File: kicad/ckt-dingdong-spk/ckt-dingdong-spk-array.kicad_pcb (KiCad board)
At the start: 2 copper layers, 292.1 x 40.6 mm, 162 parts, among them J1 SM04B-SRSS

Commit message: Changed to 5x panel
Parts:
- removed the J1 at (209.0, 40.3)
- removed the J1 at (264.8, 40.3)
- removed the J1 at (236.9, 40.3)
- removed the J1 at (181.0, 40.3)
- removed the J1 at (153.1, 40.3)
- removed the REF** at (10.1, 58.9)
- removed the REF** at (4.99, 27.6)
- removed the REF** at (247.6, 53.0)
- removed the REF** at (273.8, 27.6)
- removed the REF** at (286.9, 24.2)
- removed the REF** at (273.8, 53.0)
- removed the REF** at (6.68, 27.6)
- removed the REF** at (245.9, 53.0)
- removed the REF** at (78.2, 27.6)
- removed the REF** at (286.9, 25.1)
- removed the REF** at (77.4, 53.0)
- removed the REF** at (162.9, 53.0)
- removed the REF** at (10.1, 60.6)
- removed the REF** at (79.1, 27.6)
- removed the REF** at (10.1, 59.8)
- removed the REF** at (286.9, 20.8)
- removed the REF** at (4.99, 50.5) (x2)
- removed the REF** at (190.0, 27.6)
- removed the REF** at (245.9, 27.6)
- removed the REF** at (5.84, 27.6)
- removed the REF** at (218.8, 53.0)
- removed the REF** at (134.1, 27.6)
- removed the REF** at (3.30, 53.0)
- removed the REF** at (134.1, 53.0)
- removed the REF** at (219.6, 27.6)
- removed the REF** at (79.9, 27.6)
- removed the REF** at (135.0, 27.6)
- removed the REF** at (163.7, 27.6)
- removed the REF** at (292.0, 27.6)
- removed the REF** at (161.2, 53.0)
- removed the REF** at (293.7, 53.0)
- removed the REF** at (10.1, 23.4)
- removed the REF** at (10.1, 56.4)
- removed the REF** at (286.9, 21.7)
- removed the REF** at (7.53, 27.6)
- removed the REF** at (294.6, 27.6)
- removed the REF** at (275.5, 53.0)
- removed the REF** at (219.6, 53.0)
- removed the REF** at (162.0, 53.0)
- removed the REF** at (4.99, 30.2) (x2)
- removed the REF** at (286.9, 60.6)
- removed the REF** at (286.9, 56.4)
- removed the REF** at (217.1, 53.0)
- removed the REF** at (24.0, 53.0)
- removed the REF** at (4.14, 53.0)
- removed the REF** at (49.4, 53.0)
- removed the REF** at (292.0, 30.2) (x2)
- removed the REF** at (133.3, 27.6)
- removed the REF** at (289.5, 27.6)
- removed the REF** at (218.8, 27.6)
- removed the REF** at (274.7, 53.0)
- removed the REF** at (105.3, 27.6)
- removed the REF** at (275.5, 27.6)
- removed the REF** at (6.68, 53.0)
- removed the REF** at (273.0, 27.6)
- removed the REF** at (286.9, 22.5)
- removed the REF** at (286.9, 20.0)
- removed the REF** at (286.9, 58.9)
- removed the REF** at (10.1, 20.8)
- removed the REF** at (217.9, 27.6)
- removed the REF** at (291.2, 27.6)
- removed the REF** at (21.5, 27.6)
- removed the REF** at (191.7, 53.0)
- removed the REF** at (10.1, 55.6)
- removed the REF** at (292.9, 53.0)
- removed the REF** at (105.3, 53.0)
- removed the REF** at (51.1, 53.0)
- removed the REF** at (107.9, 27.6)
- removed the REF** at (286.9, 55.6)
- removed the REF** at (107.0, 27.6)
- removed the REF** at (274.7, 27.6)
- removed the REF** at (190.0, 53.0)
- removed the REF** at (189.1, 53.0)
- removed the REF** at (10.1, 24.2)
- removed the REF** at (286.9, 58.1)
- removed the REF** at (10.1, 20.0)
- removed the REF** at (273.0, 53.0)
- removed the REF** at (293.7, 27.6)
- removed the REF** at (78.2, 53.0)
- removed the REF** at (107.0, 53.0)
- removed the REF** at (2.45, 27.6)
- removed the REF** at (4.14, 27.6)
- removed the REF** at (190.8, 53.0)
- removed the REF** at (49.4, 27.6)
- removed the REF** at (106.2, 27.6)
- removed the REF** at (23.2, 53.0)
- removed the REF** at (246.7, 27.6)
- removed the REF** at (161.2, 27.6)
- removed the REF** at (162.0, 27.6)
- removed the REF** at (50.3, 27.6)
- removed the REF** at (294.6, 53.0)
- removed the REF** at (10.1, 21.7)
- removed the REF** at (24.0, 27.6)
- removed the REF** at (246.7, 53.0)
- removed the REF** at (286.9, 23.4)
- removed the REF** at (135.8, 27.6)
- removed the REF** at (190.8, 27.6)
- removed the REF** at (191.7, 27.6)
- removed the REF** at (107.9, 53.0)
- removed the REF** at (22.3, 53.0)
- removed the REF** at (52.0, 53.0)
- removed the REF** at (290.3, 53.0)
- removed the REF** at (52.0, 27.6)
- removed the REF** at (290.3, 27.6)
- removed the REF** at (10.1, 57.3)
- removed the REF** at (292.0, 53.0)
- removed the REF** at (289.5, 53.0)
- removed the REF** at (10.1, 22.5)
- removed the REF** at (7.53, 53.0)
- removed the REF** at (21.5, 53.0)
- removed the REF** at (291.2, 53.0)
- removed the REF** at (135.8, 53.0)
- removed the REF** at (2.45, 53.0)
- removed the REF** at (133.3, 53.0)
- removed the REF** at (106.2, 53.0)
- removed the REF** at (135.0, 53.0)
- removed the REF** at (5.84, 53.0)
- removed the REF** at (245.0, 53.0)
- removed the REF** at (247.6, 27.6)
- removed the REF** at (162.9, 27.6)
- removed the REF** at (51.1, 27.6)
- removed the REF** at (10.1, 25.1)
- removed the REF** at (189.1, 27.6)
- removed the REF** at (22.3, 27.6)
- removed the REF** at (79.1, 53.0)
- removed the REF** at (10.1, 58.1)
- removed the REF** at (79.9, 53.0)
- removed the REF** at (50.3, 53.0)
- removed the REF** at (217.9, 53.0)
- removed the REF** at (4.99, 53.0)
- removed the REF** at (23.2, 27.6)
- removed the REF** at (286.9, 57.3)
- removed the REF** at (163.7, 53.0)
- removed the REF** at (245.0, 27.6)
- removed the REF** at (3.30, 27.6)
- removed the REF** at (286.9, 59.8)
- removed the REF** at (292.9, 27.6)
- removed the REF** at (77.4, 27.6)
- removed the REF** at (217.1, 27.6)
- removed the SPK1 at (190.4, 37.8)
- removed the SPK1 at (246.3, 37.8)
- removed the SPK1 at (274.2, 37.8)
- removed the SPK1 at (218.3, 37.8)
- added REF**: NPTH, NPTH, F.Cu at (164.0, 22.6)
- added REF**: NPTH, NPTH, F.Cu at (159.8, 15.8)
- added REF**: Fiducial, Fiducial, B.Cu at (17.5, 45.5)
- added REF**: Fiducial, Fiducial, B.Cu at (17.5, 25.2)
- added REF**: Fiducial, Fiducial, B.Cu at (164.9, 25.2)
- added REF**: NPTH, NPTH, F.Cu at (34.0, 22.6)
- added REF**: NPTH, NPTH, F.Cu at (166.6, 48.0)
- added REF**: NPTH, NPTH, F.Cu at (22.6, 55.6)
- added REF**: NPTH, NPTH, F.Cu at (64.5, 48.0)
- added REF**: NPTH, NPTH, F.Cu at (22.6, 15.8)
- added REF**: NPTH, NPTH, F.Cu at (34.9, 48.0)
- added REF**: NPTH, NPTH, F.Cu at (166.6, 22.6)
- added REF**: NPTH, NPTH, F.Cu at (159.8, 55.6)
- added REF**: NPTH, NPTH, F.Cu at (162.3, 22.6)
- added REF**: NPTH, NPTH, F.Cu at (22.6, 54.8)
- added REF**: NPTH, NPTH, F.Cu at (162.3, 48.0)
- added REF**: NPTH, NPTH, F.Cu at (119.6, 48.0)
- added REF**: NPTH, NPTH, F.Cu at (159.8, 54.8)
- added REF**: NPTH, NPTH, F.Cu at (145.8, 48.0)
- added REF**: NPTH, NPTH, F.Cu at (15.8, 22.6)
- added REF**: NPTH, NPTH, F.Cu at (119.6, 22.6)
- added REF**: NPTH, NPTH, F.Cu at (16.7, 48.0)
- added REF**: NPTH, NPTH, F.Cu at (35.7, 48.0)
- added REF**: NPTH, NPTH, F.Cu at (20.1, 22.6)
- added REF**: NPTH, NPTH, F.Cu at (92.5, 22.6)
- added REF**: NPTH, NPTH, F.Cu at (22.6, 17.5)
- added REF**: NPTH, NPTH, F.Cu at (22.6, 18.4)
- added REF**: NPTH, NPTH, F.Cu at (159.8, 50.6)
- added REF**: NPTH, NPTH, F.Cu at (118.7, 22.6)
- added REF**: NPTH, NPTH, F.Cu at (62.0, 48.0)
- added REF**: NPTH, NPTH, F.Cu at (159.8, 53.1)
- added REF**: NPTH, NPTH, F.Cu at (159.8, 53.9)
- added REF**: NPTH, NPTH, F.Cu at (165.7, 22.6)
- added REF**: NPTH, NPTH, F.Cu at (64.5, 22.6)
- added REF**: NPTH, NPTH, F.Cu at (165.7, 48.0)
- added REF**: NPTH, NPTH, F.Cu at (15.0, 22.6)
- added REF**: NPTH, NPTH, F.Cu at (148.3, 22.6)
- added REF**: NPTH, NPTH, F.Cu at (16.7, 22.6)
- added REF**: NPTH, NPTH, F.Cu at (147.5, 22.6)
- added REF**: NPTH, NPTH, F.Cu at (163.2, 22.6)
- added REF**: NPTH, NPTH, F.Cu at (145.8, 22.6)
- added REF**: NPTH, NPTH, F.Cu at (146.7, 48.0)
- added REF**: NPTH, NPTH, F.Cu at (63.7, 48.0)
- added REF**: NPTH, NPTH, F.Cu at (22.6, 19.2)
- added REF**: NPTH, NPTH, F.Cu at (62.0, 22.6)
- added REF**: NPTH, NPTH, F.Cu at (164.0, 48.0)
- added REF**: NPTH, NPTH, F.Cu at (117.9, 48.0)
- added REF**: NPTH, NPTH, F.Cu at (90.8, 22.6)
- added REF**: NPTH, NPTH, F.Cu at (62.8, 48.0)
- added REF**: NPTH, NPTH, F.Cu at (120.4, 22.6)
- added REF**: NPTH, NPTH, F.Cu at (90.8, 48.0)
- added REF**: NPTH, NPTH, F.Cu at (159.8, 18.4)
- added REF**: NPTH, NPTH, F.Cu at (18.4, 48.0)
- added REF**: NPTH, NPTH, F.Cu at (22.6, 16.7)
- added REF**: Fiducial, Fiducial, F.Cu at (164.9, 25.2)
- added REF**: NPTH, NPTH, F.Cu at (159.8, 52.3)
- added REF**: NPTH, NPTH, F.Cu at (22.6, 15.0)
- added REF**: NPTH, NPTH, F.Cu at (15.8, 48.0)
- added REF**: NPTH, NPTH, F.Cu at (117.9, 22.6)
- added REF**: NPTH, NPTH, F.Cu at (20.1, 48.0)
- added REF**: NPTH, NPTH, F.Cu at (159.8, 16.7)
- added REF**: NPTH, NPTH, F.Cu at (164.9, 22.6)
- added REF**: NPTH, NPTH, F.Cu at (22.6, 51.4)
- added REF**: NPTH, NPTH, F.Cu at (22.6, 53.9)
- added REF**: NPTH, NPTH, F.Cu at (63.7, 22.6)
- added REF**: NPTH, NPTH, F.Cu at (17.5, 22.6)
- added REF**: NPTH, NPTH, F.Cu at (159.8, 19.2)
- added REF**: NPTH, NPTH, F.Cu at (19.2, 48.0)
- added REF**: Fiducial, Fiducial, F.Cu at (17.5, 25.2)
- added REF**: NPTH, NPTH, F.Cu at (147.5, 48.0)
- added REF**: NPTH, NPTH, F.Cu at (89.9, 22.6)
- added REF**: NPTH, NPTH, F.Cu at (15.0, 48.0)
- added REF**: NPTH, NPTH, F.Cu at (62.8, 22.6)
- added REF**: NPTH, NPTH, F.Cu at (36.6, 22.6)
- added REF**: NPTH, NPTH, F.Cu at (159.8, 20.1)
- added REF**: NPTH, NPTH, F.Cu at (148.3, 48.0)
- added REF**: NPTH, NPTH, F.Cu at (17.5, 48.0)
- added REF**: NPTH, NPTH, F.Cu at (22.6, 52.3)
- added REF**: NPTH, NPTH, F.Cu at (34.9, 22.6)
- added REF**: NPTH, NPTH, F.Cu at (19.2, 22.6)
- added REF**: NPTH, NPTH, F.Cu at (159.8, 51.4)
- added REF**: NPTH, NPTH, F.Cu at (164.9, 48.0)
- added REF**: NPTH, NPTH, F.Cu at (159.8, 15.0)
- added REF**: NPTH, NPTH, F.Cu at (22.6, 50.6)
- added REF**: NPTH, NPTH, F.Cu at (146.7, 22.6)
- added REF**: NPTH, NPTH, F.Cu at (92.5, 48.0)
- added REF**: NPTH, NPTH, F.Cu at (22.6, 20.1)
- added REF**: NPTH, NPTH, F.Cu at (118.7, 48.0)
- added REF**: NPTH, NPTH, F.Cu at (18.4, 22.6)
- added REF**: NPTH, NPTH, F.Cu at (89.9, 48.0)
- added REF**: NPTH, NPTH, F.Cu at (163.2, 48.0)
- added REF**: NPTH, NPTH, F.Cu at (36.6, 48.0)
- added REF**: NPTH, NPTH, F.Cu at (34.0, 48.0)
- added REF**: NPTH, NPTH, F.Cu at (91.6, 48.0)
- added REF**: NPTH, NPTH, F.Cu at (22.6, 53.1)
- added REF**: NPTH, NPTH, F.Cu at (91.6, 22.6)
- added REF**: NPTH, NPTH, F.Cu at (167.4, 22.6)
- added REF**: NPTH, NPTH, F.Cu at (120.4, 48.0)
- added REF**: NPTH, NPTH, F.Cu at (35.7, 22.6)
- added REF**: NPTH, NPTH, F.Cu at (167.4, 48.0)
- added REF**: NPTH, NPTH, F.Cu at (159.8, 17.5)
- REF**: renamed from SPK1; value Speaker -> Fiducial; footprint ISE_Generic:Speaker_13x18 -> Fiducial; moved to F.Cu
- moved REF** 145.1 mm to (17.5, 45.5), turned to 0 degrees
- moved J1 13.5 mm to (109.7, 35.3)
- moved J1 13.5 mm to (81.8, 35.3)
- moved SPK1 13.5 mm to (147.1, 32.8)
- moved J1 13.5 mm to (53.9, 35.3)
- moved J1 13.5 mm to (25.9, 35.3)
- moved SPK1 13.5 mm to (35.3, 32.8)
- moved SPK1 13.5 mm to (119.1, 32.8)
- moved SPK1 13.5 mm to (91.2, 32.8)
- moved SPK1 13.5 mm to (63.3, 32.8)
- moved J1 13.5 mm to (137.7, 35.3)
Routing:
- net Board_9-Net-(SPK1-Pad1): track 35.5 -> 0.00 mm, vias 3 -> 0
- net Board_8-Net-(SPK1-Pad1): track 35.5 -> 0.00 mm, vias 3 -> 0
- net Board_7-Net-(SPK1-Pad1): track 35.5 -> 0.00 mm, vias 3 -> 0
- net Board_6-Net-(SPK1-Pad1): track 35.5 -> 0.00 mm, vias 3 -> 0
- net Board_5-Net-(SPK1-Pad1): track 35.5 -> 0.00 mm, vias 3 -> 0
- net Board_9-Net-(SPK1-Pad2): track 21.5 -> 0.00 mm, vias 3 -> 0
- net Board_8-Net-(SPK1-Pad2): track 21.5 -> 0.00 mm, vias 3 -> 0
- net Board_7-Net-(SPK1-Pad2): track 21.5 -> 0.00 mm, vias 3 -> 0
- net Board_6-Net-(SPK1-Pad2): track 21.5 -> 0.00 mm, vias 3 -> 0
- net Board_5-Net-(SPK1-Pad2): track 21.5 -> 0.00 mm, vias 3 -> 0
- removed copper zone on F.Cu, net Board_5-/MP
- removed copper zone on F.Cu, net Board_6-/MP
- removed copper zone on F.Cu, net Board_7-/MP
- removed copper zone on F.Cu, net Board_8-/MP
- removed copper zone on F.Cu, net Board_9-/MP
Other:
- board size 292.1 x 40.6 mm -> 152.4 x 40.6 mm

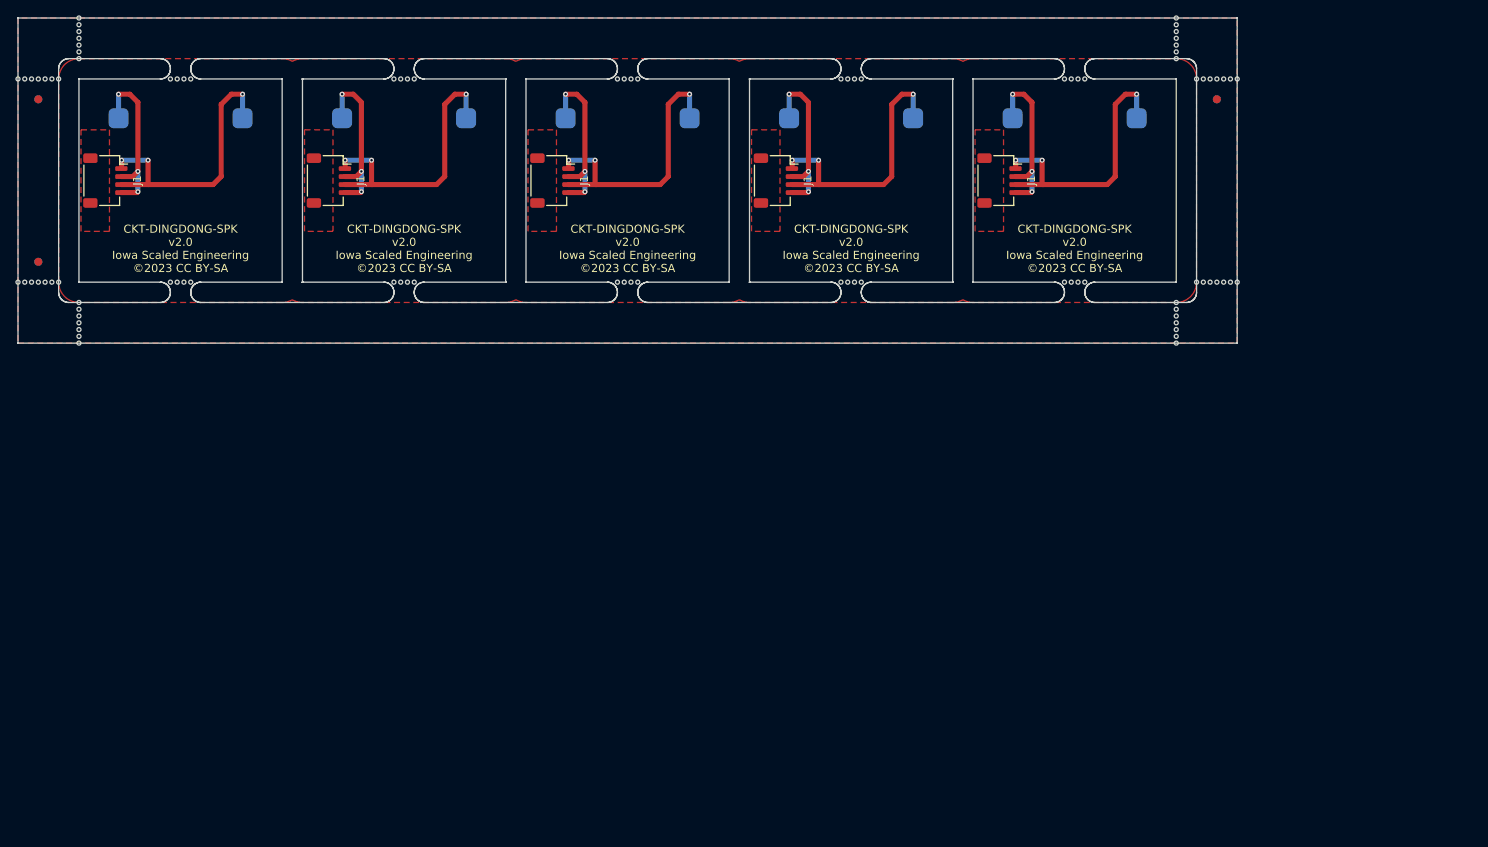
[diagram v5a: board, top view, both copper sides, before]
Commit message: Updated panelization
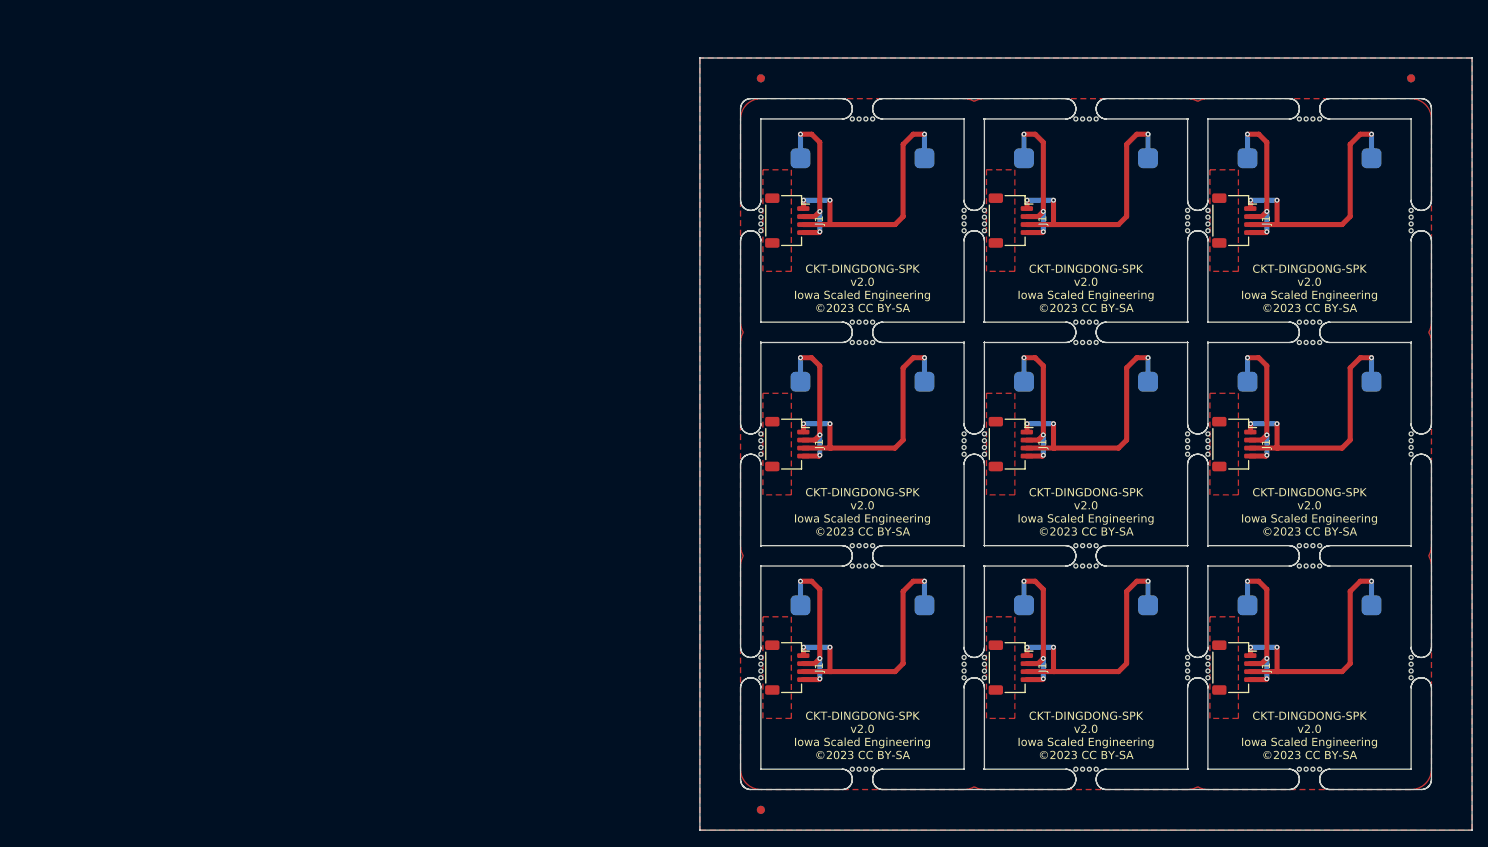
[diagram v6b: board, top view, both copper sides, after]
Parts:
- removed the REF** at (164.0, 22.6)
- removed the REF** at (159.8, 15.8)
- removed the REF** at (17.5, 45.5)
- removed the REF** at (17.5, 25.2) (x2)
- removed the REF** at (164.9, 25.2) (x2)
- removed the REF** at (34.0, 22.6)
- removed the REF** at (166.6, 48.0)
- removed the REF** at (22.6, 55.6)
- removed the REF** at (64.5, 48.0)
- removed the REF** at (22.6, 15.8)
- removed the REF** at (34.9, 48.0)
- removed the REF** at (166.6, 22.6)
- removed the REF** at (159.8, 55.6)
- removed the REF** at (162.3, 22.6)
- removed the REF** at (22.6, 54.8)
- removed the REF** at (162.3, 48.0)
- removed the REF** at (119.6, 48.0)
- removed the REF** at (159.8, 54.8)
- removed the REF** at (145.8, 48.0)
- removed the REF** at (15.8, 22.6)
- removed the REF** at (119.6, 22.6)
- removed the REF** at (16.7, 48.0)
- removed the REF** at (35.7, 48.0)
- removed the REF** at (20.1, 22.6)
- removed the REF** at (92.5, 22.6)
- removed the REF** at (22.6, 17.5)
- removed the REF** at (22.6, 18.4)
- removed the REF** at (159.8, 50.6)
- removed the REF** at (118.7, 22.6)
- removed the REF** at (62.0, 48.0)
- removed the REF** at (159.8, 53.1)
- removed the REF** at (159.8, 53.9)
- removed the REF** at (165.7, 22.6)
- removed the REF** at (64.5, 22.6)
- removed the REF** at (165.7, 48.0)
- removed the REF** at (15.0, 22.6)
- removed the REF** at (148.3, 22.6)
- removed the REF** at (16.7, 22.6)
- removed the REF** at (147.5, 22.6)
- removed the REF** at (163.2, 22.6)
- removed the REF** at (145.8, 22.6)
- removed the REF** at (146.7, 48.0)
- removed the REF** at (63.7, 48.0)
- removed the REF** at (22.6, 19.2)
- removed the REF** at (62.0, 22.6)
- removed the REF** at (164.0, 48.0)
- removed the REF** at (117.9, 48.0)
- removed the REF** at (90.8, 22.6)
- removed the REF** at (62.8, 48.0)
- removed the REF** at (120.4, 22.6)
- removed the REF** at (90.8, 48.0)
- removed the REF** at (159.8, 18.4)
- removed the REF** at (18.4, 48.0)
- removed the REF** at (22.6, 16.7)
- removed the REF** at (159.8, 52.3)
- removed the REF** at (22.6, 15.0)
- removed the REF** at (15.8, 48.0)
- removed the REF** at (117.9, 22.6)
- removed the REF** at (20.1, 48.0)
- removed the REF** at (159.8, 16.7)
- removed the REF** at (164.9, 22.6)
- removed the REF** at (22.6, 51.4)
- removed the REF** at (22.6, 53.9)
- removed the REF** at (63.7, 22.6)
- removed the REF** at (17.5, 22.6)
- removed the REF** at (159.8, 19.2)
- removed the REF** at (19.2, 48.0)
- removed the REF** at (147.5, 48.0)
- removed the REF** at (89.9, 22.6)
- removed the REF** at (15.0, 48.0)
- removed the REF** at (62.8, 22.6)
- removed the REF** at (36.6, 22.6)
- removed the REF** at (159.8, 20.1)
- removed the REF** at (148.3, 48.0)
- removed the REF** at (17.5, 48.0)
- removed the REF** at (22.6, 52.3)
- removed the REF** at (34.9, 22.6)
- removed the REF** at (19.2, 22.6)
- removed the REF** at (159.8, 51.4)
- removed the REF** at (164.9, 48.0)
- removed the REF** at (159.8, 15.0)
- removed the REF** at (22.6, 50.6)
- removed the REF** at (146.7, 22.6)
- removed the REF** at (92.5, 48.0)
- removed the REF** at (22.6, 20.1)
- removed the REF** at (118.7, 48.0)
- removed the REF** at (18.4, 22.6)
- removed the REF** at (89.9, 48.0)
- removed the REF** at (163.2, 48.0)
- removed the REF** at (36.6, 48.0)
- removed the REF** at (34.0, 48.0)
- removed the REF** at (91.6, 48.0)
- removed the REF** at (22.6, 53.1)
- removed the REF** at (91.6, 22.6)
- removed the REF** at (167.4, 22.6)
- removed the REF** at (120.4, 48.0)
- removed the REF** at (35.7, 22.6)
- removed the REF** at (167.4, 48.0)
- removed the REF** at (159.8, 17.5)
- added J1: SM04B-SRSS, Connector_JST:JST_SH_SM04B-SRSS-TB_1x04-1MP_P1.00mm_Horizontal, F.Cu at (139.1, 96.2)
- added J1: SM04B-SRSS, Connector_JST:JST_SH_SM04B-SRSS-TB_1x04-1MP_P1.00mm_Horizontal, F.Cu at (167.0, 96.2)
- added J1: SM04B-SRSS, Connector_JST:JST_SH_SM04B-SRSS-TB_1x04-1MP_P1.00mm_Horizontal, F.Cu at (111.2, 96.2)
- added J1: SM04B-SRSS, Connector_JST:JST_SH_SM04B-SRSS-TB_1x04-1MP_P1.00mm_Horizontal, F.Cu at (167.0, 68.3)
- added REF**: NPTH, NPTH, F.Cu at (133.3, 40.7)
- added REF**: NPTH, NPTH, F.Cu at (107.9, 95.8)
- added REF**: NPTH, NPTH, F.Cu at (120.1, 83.5)
- added REF**: NPTH, NPTH, F.Cu at (135.8, 69.5)
- added REF**: NPTH, NPTH, F.Cu at (148.1, 53.0)
- added REF**: NPTH, NPTH, F.Cu at (176.9, 83.5)
- added REF**: NPTH, NPTH, F.Cu at (163.7, 68.7)
- added REF**: NPTH, NPTH, F.Cu at (135.8, 41.6)
- added REF**: NPTH, NPTH, F.Cu at (107.9, 67.0)
- added REF**: NPTH, NPTH, F.Cu at (121.8, 108.9)
- added REF**: NPTH, NPTH, F.Cu at (121.8, 55.6)
- added REF**: NPTH, NPTH, F.Cu at (148.1, 83.5)
- added REF**: NPTH, NPTH, F.Cu at (107.9, 67.8)
- added REF**: NPTH, NPTH, F.Cu at (121.8, 27.6)
- added REF**: NPTH, NPTH, F.Cu at (175.2, 81.0)
- added REF**: NPTH, NPTH, F.Cu at (119.3, 27.6)
- added REF**: NPTH, NPTH, F.Cu at (119.3, 83.5)
- added REF**: NPTH, NPTH, F.Cu at (107.9, 69.5)
- added REF**: NPTH, NPTH, F.Cu at (135.8, 68.7)
- added REF**: NPTH, NPTH, F.Cu at (189.1, 97.5)
- added REF**: NPTH, NPTH, F.Cu at (148.9, 27.6)
- added REF**: NPTH, NPTH, F.Cu at (147.2, 27.6)
- added REF**: NPTH, NPTH, F.Cu at (107.9, 39.9)
- added REF**: NPTH, NPTH, F.Cu at (148.9, 108.9)
- added REF**: NPTH, NPTH, F.Cu at (135.8, 95.8)
- added REF**: NPTH, NPTH, F.Cu at (135.8, 97.5)
- added REF**: NPTH, NPTH, F.Cu at (133.3, 95.8)
- added REF**: NPTH, NPTH, F.Cu at (161.2, 39.9)
- added REF**: NPTH, NPTH, F.Cu at (189.1, 39.9)
- added REF**: NPTH, NPTH, F.Cu at (161.2, 96.6)
- added REF**: NPTH, NPTH, F.Cu at (133.3, 94.9)
- added REF**: NPTH, NPTH, F.Cu at (149.8, 53.0)
- added REF**: NPTH, NPTH, F.Cu at (148.9, 83.5)
- added REF**: NPTH, NPTH, F.Cu at (189.1, 67.0)
- added REF**: NPTH, NPTH, F.Cu at (163.7, 39.9)
- added REF**: NPTH, NPTH, F.Cu at (147.2, 81.0)
- added REF**: NPTH, NPTH, F.Cu at (147.2, 53.0)
- added REF**: NPTH, NPTH, F.Cu at (189.1, 67.8)
- added REF**: NPTH, NPTH, F.Cu at (177.7, 81.0)
- added REF**: NPTH, NPTH, F.Cu at (107.9, 39.0)
- added REF**: NPTH, NPTH, F.Cu at (163.7, 40.7)
- added REF**: NPTH, NPTH, F.Cu at (177.7, 83.5)
- added REF**: NPTH, NPTH, F.Cu at (135.8, 40.7)
- added REF**: NPTH, NPTH, F.Cu at (135.8, 39.9)
- added REF**: NPTH, NPTH, F.Cu at (121.0, 53.0)
- added REF**: NPTH, NPTH, F.Cu at (148.1, 27.6)
- added REF**: NPTH, NPTH, F.Cu at (120.1, 53.0)
- added REF**: NPTH, NPTH, F.Cu at (163.7, 95.8)
- added REF**: NPTH, NPTH, F.Cu at (189.1, 94.9)
- added REF**: NPTH, NPTH, F.Cu at (133.3, 97.5)
- added REF**: NPTH, NPTH, F.Cu at (161.2, 94.9)
- added REF**: NPTH, NPTH, F.Cu at (176.0, 81.0)
- added REF**: NPTH, NPTH, F.Cu at (163.7, 67.0)
- added REF**: NPTH, NPTH, F.Cu at (121.0, 27.6)
- added REF**: Fiducial, Fiducial, B.Cu at (107.9, 114.0)
- added REF**: Fiducial, Fiducial, B.Cu at (107.9, 22.5)
- added REF**: NPTH, NPTH, F.Cu at (107.9, 40.7)
- added REF**: Fiducial, Fiducial, B.Cu at (189.1, 22.5)
- added REF**: NPTH, NPTH, F.Cu at (175.2, 55.6)
- added REF**: NPTH, NPTH, F.Cu at (135.8, 96.6)
- added REF**: NPTH, NPTH, F.Cu at (176.0, 83.5)
- added REF**: NPTH, NPTH, F.Cu at (177.7, 55.6)
- added REF**: NPTH, NPTH, F.Cu at (175.2, 108.9)
- added REF**: NPTH, NPTH, F.Cu at (176.0, 53.0)
- added REF**: NPTH, NPTH, F.Cu at (135.8, 67.0)
- added REF**: NPTH, NPTH, F.Cu at (107.9, 94.9)
- added REF**: NPTH, NPTH, F.Cu at (161.2, 39.0)
- added REF**: NPTH, NPTH, F.Cu at (133.3, 96.6)
- added REF**: NPTH, NPTH, F.Cu at (176.9, 27.6)
- added REF**: NPTH, NPTH, F.Cu at (163.7, 96.6)
- added REF**: NPTH, NPTH, F.Cu at (175.2, 83.5)
- added REF**: NPTH, NPTH, F.Cu at (189.1, 96.6)
- added REF**: NPTH, NPTH, F.Cu at (120.1, 108.9)
- added REF**: NPTH, NPTH, F.Cu at (147.2, 83.5)
- added REF**: NPTH, NPTH, F.Cu at (161.2, 95.8)
- added REF**: NPTH, NPTH, F.Cu at (161.2, 97.5)
- added REF**: NPTH, NPTH, F.Cu at (120.1, 27.6)
- added REF**: NPTH, NPTH, F.Cu at (148.1, 55.6)
- added REF**: NPTH, NPTH, F.Cu at (107.9, 96.6)
- added REF**: NPTH, NPTH, F.Cu at (121.0, 108.9)
- added REF**: NPTH, NPTH, F.Cu at (148.1, 108.9)
- added REF**: NPTH, NPTH, F.Cu at (133.3, 67.0)
- added REF**: Fiducial, Fiducial, F.Cu at (107.9, 114.0)
- added REF**: NPTH, NPTH, F.Cu at (176.9, 55.6)
- added REF**: NPTH, NPTH, F.Cu at (135.8, 39.0)
- added REF**: NPTH, NPTH, F.Cu at (161.2, 68.7)
- added REF**: NPTH, NPTH, F.Cu at (189.1, 95.8)
- added REF**: NPTH, NPTH, F.Cu at (119.3, 55.6)
- added REF**: NPTH, NPTH, F.Cu at (133.3, 68.7)
- added REF**: NPTH, NPTH, F.Cu at (161.2, 67.0)
- added REF**: NPTH, NPTH, F.Cu at (163.7, 69.5)
- added REF**: NPTH, NPTH, F.Cu at (133.3, 39.9)
- added REF**: NPTH, NPTH, F.Cu at (161.2, 69.5)
- added REF**: NPTH, NPTH, F.Cu at (120.1, 55.6)
- added REF**: NPTH, NPTH, F.Cu at (119.3, 53.0)
- added REF**: NPTH, NPTH, F.Cu at (121.8, 53.0)
- added REF**: NPTH, NPTH, F.Cu at (176.9, 53.0)
- added REF**: NPTH, NPTH, F.Cu at (149.8, 108.9)
- added REF**: NPTH, NPTH, F.Cu at (121.8, 81.0)
- added REF**: Fiducial, Fiducial, F.Cu at (189.1, 22.5)
- added REF**: NPTH, NPTH, F.Cu at (147.2, 55.6)
- added REF**: NPTH, NPTH, F.Cu at (121.8, 83.5)
- added REF**: NPTH, NPTH, F.Cu at (176.0, 27.6)
- added REF**: NPTH, NPTH, F.Cu at (147.2, 108.9)
- added REF**: NPTH, NPTH, F.Cu at (163.7, 41.6)
- added REF**: NPTH, NPTH, F.Cu at (176.0, 108.9)
- added REF**: NPTH, NPTH, F.Cu at (148.9, 53.0)
- added REF**: NPTH, NPTH, F.Cu at (133.3, 39.0)
- added REF**: NPTH, NPTH, F.Cu at (119.3, 108.9)
- added REF**: NPTH, NPTH, F.Cu at (177.7, 27.6)
- added REF**: NPTH, NPTH, F.Cu at (177.7, 53.0)
- added REF**: NPTH, NPTH, F.Cu at (189.1, 68.7)
- added REF**: NPTH, NPTH, F.Cu at (107.9, 97.5)
- added REF**: NPTH, NPTH, F.Cu at (163.7, 39.0)
- added REF**: NPTH, NPTH, F.Cu at (161.2, 41.6)
- added REF**: NPTH, NPTH, F.Cu at (120.1, 81.0)
- added REF**: Fiducial, Fiducial, F.Cu at (107.9, 22.5)
- added REF**: NPTH, NPTH, F.Cu at (121.0, 55.6)
- added REF**: NPTH, NPTH, F.Cu at (149.8, 83.5)
- added REF**: NPTH, NPTH, F.Cu at (135.8, 94.9)
- added REF**: NPTH, NPTH, F.Cu at (107.9, 41.6)
- added REF**: NPTH, NPTH, F.Cu at (148.9, 81.0)
- added REF**: NPTH, NPTH, F.Cu at (121.0, 83.5)
- added REF**: NPTH, NPTH, F.Cu at (133.3, 67.8)
- added REF**: NPTH, NPTH, F.Cu at (163.7, 67.8)
- added REF**: NPTH, NPTH, F.Cu at (148.1, 81.0)
- added REF**: NPTH, NPTH, F.Cu at (189.1, 41.6)
- added REF**: NPTH, NPTH, F.Cu at (189.1, 40.7)
- added REF**: NPTH, NPTH, F.Cu at (177.7, 108.9)
- added REF**: NPTH, NPTH, F.Cu at (161.2, 40.7)
- added REF**: NPTH, NPTH, F.Cu at (161.2, 67.8)
- added REF**: NPTH, NPTH, F.Cu at (175.2, 27.6)
- added REF**: NPTH, NPTH, F.Cu at (176.9, 81.0)
- added REF**: NPTH, NPTH, F.Cu at (149.8, 81.0)
- added REF**: NPTH, NPTH, F.Cu at (189.1, 69.5)
- added REF**: NPTH, NPTH, F.Cu at (149.8, 55.6)
- added REF**: NPTH, NPTH, F.Cu at (149.8, 27.6)
- added REF**: NPTH, NPTH, F.Cu at (176.9, 108.9)
- added REF**: NPTH, NPTH, F.Cu at (175.2, 53.0)
- added REF**: NPTH, NPTH, F.Cu at (133.3, 41.6)
- added REF**: NPTH, NPTH, F.Cu at (189.1, 39.0)
- added REF**: NPTH, NPTH, F.Cu at (121.0, 81.0)
- added REF**: NPTH, NPTH, F.Cu at (107.9, 68.7)
- added REF**: NPTH, NPTH, F.Cu at (163.7, 97.5)
- added REF**: NPTH, NPTH, F.Cu at (119.3, 81.0)
- added REF**: NPTH, NPTH, F.Cu at (135.8, 67.8)
- added REF**: NPTH, NPTH, F.Cu at (163.7, 94.9)
- added REF**: NPTH, NPTH, F.Cu at (148.9, 55.6)
- added REF**: NPTH, NPTH, F.Cu at (176.0, 55.6)
- added REF**: NPTH, NPTH, F.Cu at (133.3, 69.5)
- added SPK1: Speaker, ISE_Generic:Speaker_13x18, B.Cu at (120.6, 93.7)
- added SPK1: Speaker, ISE_Generic:Speaker_13x18, B.Cu at (176.4, 93.7)
- added SPK1: Speaker, ISE_Generic:Speaker_13x18, B.Cu at (148.5, 93.7)
- SPK1: renamed from REF**; value Fiducial -> Speaker; footprint Fiducial -> ISE_Generic:Speaker_13x18; moved to B.Cu
- moved SPK1 160.2 mm to (176.4, 65.7), turned to 180 degrees
- moved J1 85.4 mm to (111.2, 40.3)
- moved J1 85.4 mm to (139.1, 40.3)
- moved SPK1 85.4 mm to (120.6, 37.8)
- moved SPK1 85.4 mm to (148.5, 37.8)
- moved J1 85.4 mm to (167.0, 40.3)
- moved SPK1 85.4 mm to (176.4, 37.8)
- moved J1 33.0 mm to (139.1, 68.3)
- moved J1 33.0 mm to (111.2, 68.3)
- moved SPK1 33.0 mm to (120.6, 65.7)
- moved SPK1 33.0 mm to (148.5, 65.7)
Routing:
- net Board_7-Net-(SPK1-Pad1): track 0.00 -> 35.5 mm, vias 0 -> 3
- net Board_8-Net-(SPK1-Pad1): track 0.00 -> 35.5 mm, vias 0 -> 3
- net Board_6-Net-(SPK1-Pad1): track 0.00 -> 35.5 mm, vias 0 -> 3
- net Board_5-Net-(SPK1-Pad1): track 0.00 -> 35.5 mm, vias 0 -> 3
- net Board_7-Net-(SPK1-Pad2): track 0.00 -> 21.5 mm, vias 0 -> 3
- net Board_8-Net-(SPK1-Pad2): track 0.00 -> 21.5 mm, vias 0 -> 3
- net Board_6-Net-(SPK1-Pad2): track 0.00 -> 21.5 mm, vias 0 -> 3
- net Board_5-Net-(SPK1-Pad2): track 0.00 -> 21.5 mm, vias 0 -> 3
- added copper zone on F.Cu, net Board_5-/MP
- added copper zone on F.Cu, net Board_6-/MP
- added copper zone on F.Cu, net Board_7-/MP
- added copper zone on F.Cu, net Board_8-/MP
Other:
- board size 152.4 x 40.6 mm -> 96.5 x 96.5 mm
